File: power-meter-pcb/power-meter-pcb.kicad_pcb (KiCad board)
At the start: 4 copper layers, 23 x 51.5 mm, 55 parts, among them J1 Crank interconnect, J2 Debug, J3 USB4120-03-C_REVA, J4 Battery, J5 Side A, J6 Side B, J7 Spare GPIO pins, Q3 AS2302, SW1 EN, SW2 BOOT, U1 TPS613221ADBV, U2 P3T1755, U4 TPD3E001DRLR, U7 ADS1232IPW, U8 ESP32-S3-MINI-1

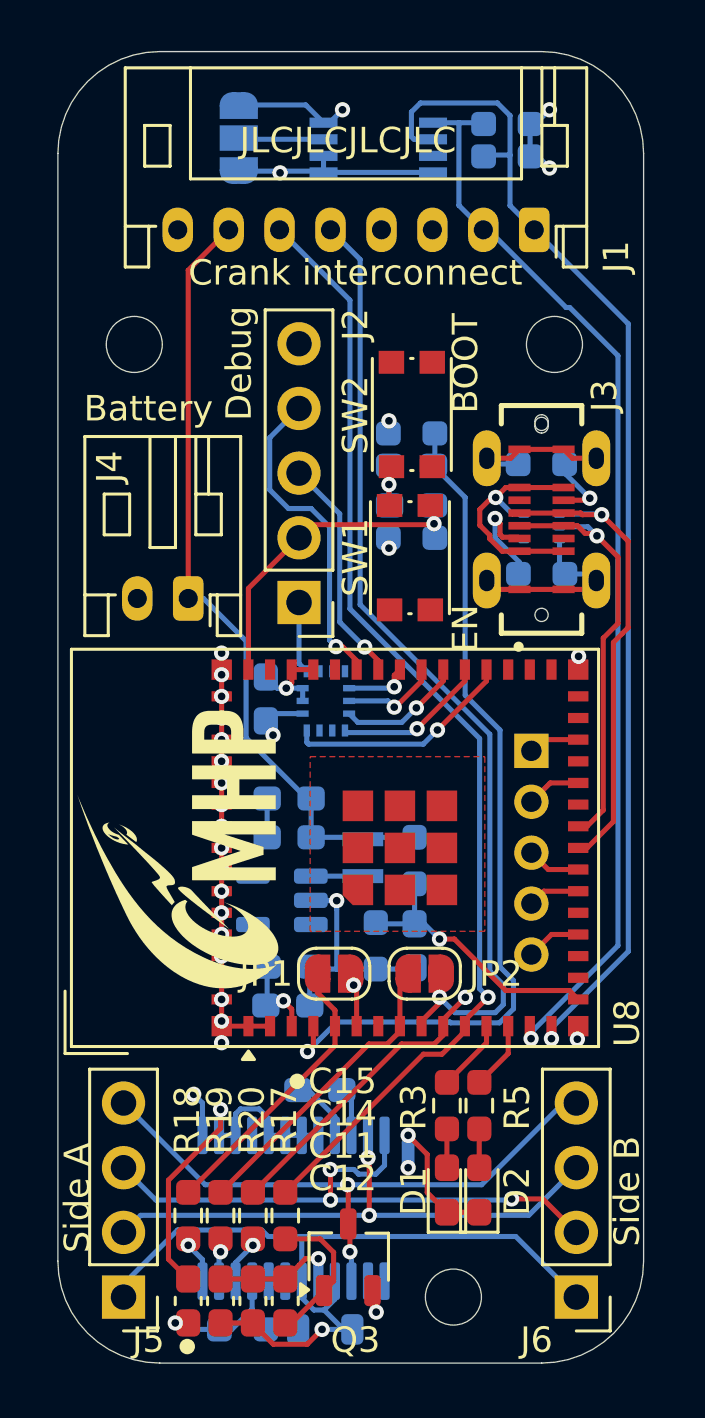
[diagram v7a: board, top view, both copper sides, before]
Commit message: Added LED driven by temp sensor, updated numbering
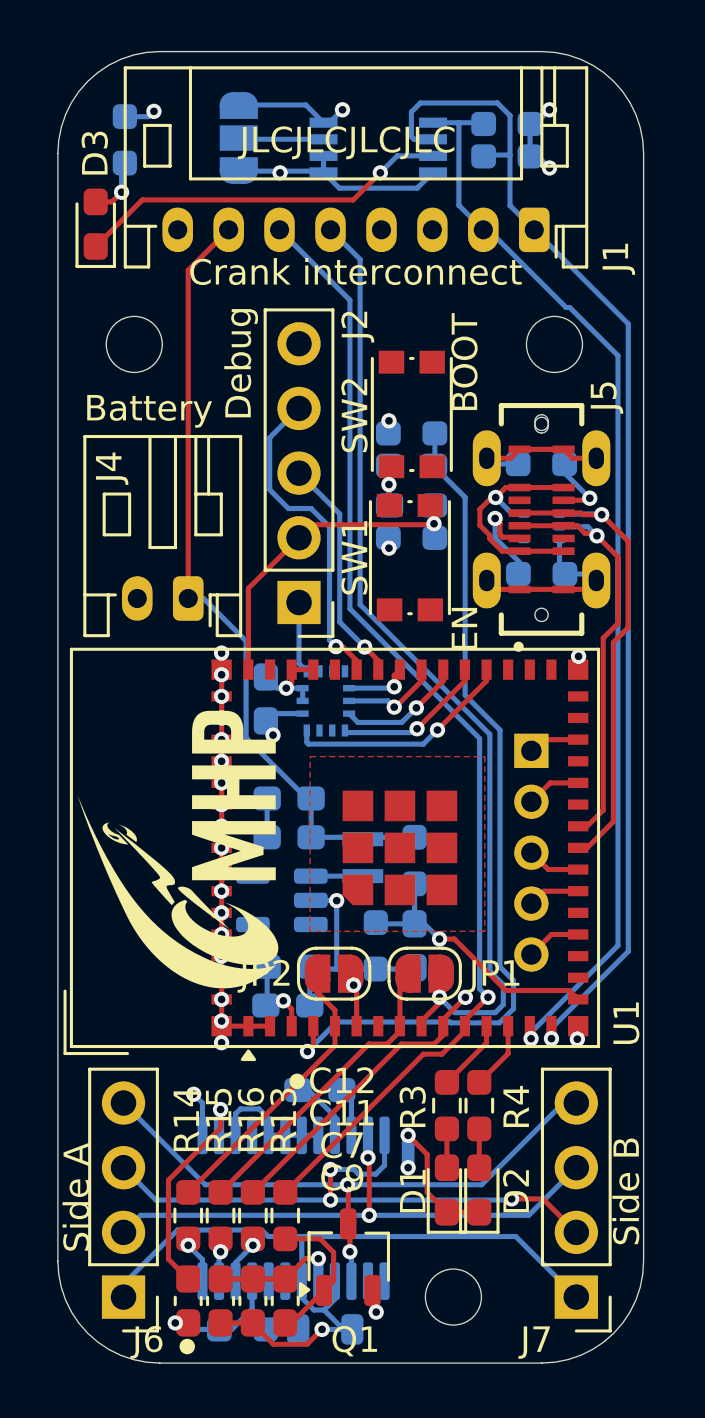
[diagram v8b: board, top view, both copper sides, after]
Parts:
- added D3: LED, LED_SMD:LED_0603_1608Metric_Pad1.05x0.95mm_HandSolder, F.Cu at (145.4, 73.9)
- added R5: 320, Resistor_SMD:R_0603_1608Metric_Pad0.98x0.95mm_HandSolder, B.Cu at (146.5, 70.6)
- renumbered C13 to C10, C14 to C11, C15 to C12, C16 to C13, C5 to C3, C7 to C4, C8 to C5, C10 to C6, C11 to C7, C9 to C8, C12 to C9, J7 to J3, J3 to J5, J5 to J6, J6 to J7, JP2 to JP1, JP1 to JP2, NT2 to NT1, Q3 to Q1, R16 to R10, R14 to R11, R15 to R12, R17 to R13, R18 to R14, R19 to R15, R20 to R16, R5 to R4, R4 to R6, R6 to R7, R11 to R9, U8 to U1, U1 to U3, U7 to U5
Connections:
- U2 pad 3: unconnected-(U2-ALERT-Pad3) -> /LED3
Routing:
- net /LED3: track 0.00 -> 14.7 mm, vias 0 -> 2
- net (no net): track 0.00 -> 2.37 mm
- net Net-(D3-K): track 0.00 -> 1.23 mm, vias 0 -> 1
- net GNDD: track 77.9 -> 78.4 mm
